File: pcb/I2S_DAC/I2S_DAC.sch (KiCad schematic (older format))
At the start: 36 parts, among them J1 AudioPlug3, J2 Conn_01x06, J3 Conn_01x09, U1 MIC5225-3.3YM5, U2 UDA1334ATS

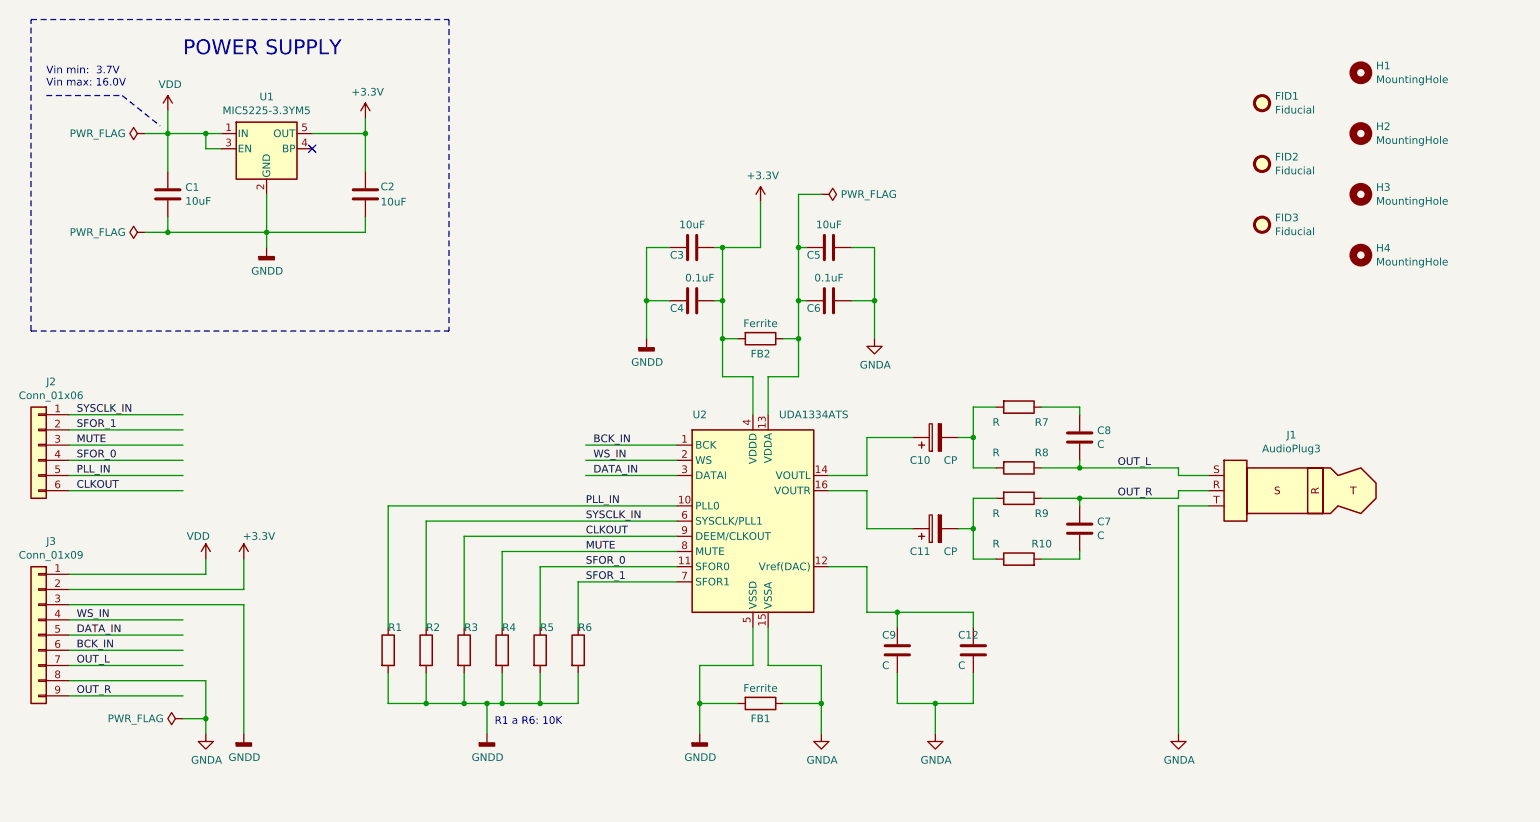
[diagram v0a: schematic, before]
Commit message: edicion de licencia en SCH
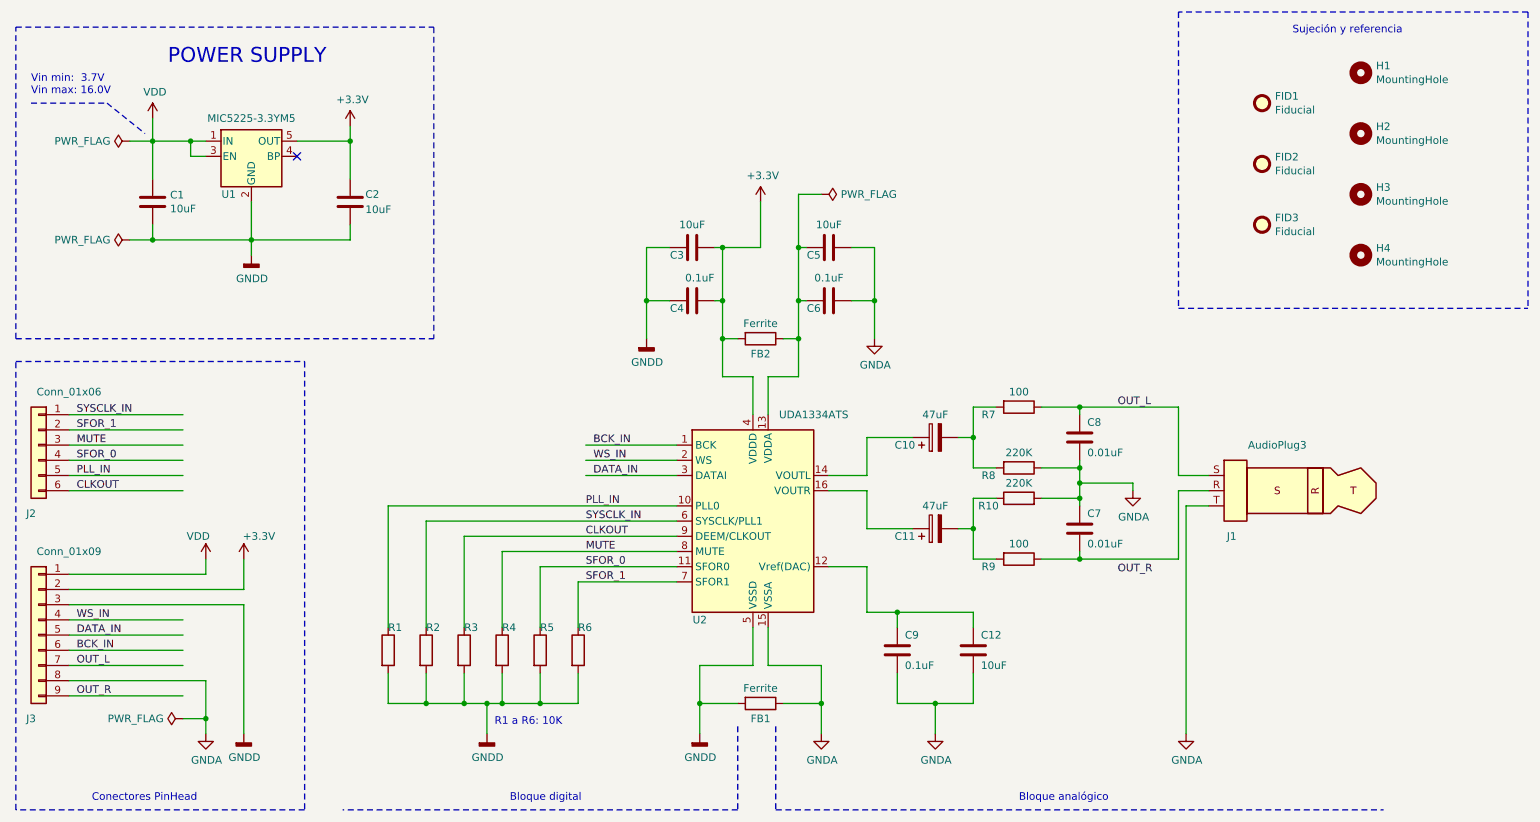
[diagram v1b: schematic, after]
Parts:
- C1, C2, C3, C4, C5, C6: footprint (none) -> Capacitor_SMD:C_0805_2012Metric
- C10, C11: value CP -> 47uF; footprint (none) -> Capacitor_SMD:C_Elec_4x5.4
- C12: value C -> 10uF; footprint (none) -> Capacitor_SMD:C_0805_2012Metric
- C7, C8: value C -> 0.01uF; footprint (none) -> Capacitor_SMD:C_0805_2012Metric
- C9: value C -> 0.1uF; footprint (none) -> Capacitor_SMD:C_0805_2012Metric
- FB1, FB2: footprint (none) -> Inductor_SMD:L_0805_2012Metric
- J2: footprint (none) -> Connector_PinHeader_2.54mm:PinHeader_1x06_P2.54mm_Vertical
- J3: footprint (none) -> Connector_PinHeader_2.54mm:PinHeader_1x09_P2.54mm_Vertical
- R1, R2, R3, R4, R5, R6: footprint (none) -> Resistor_SMD:R_0805_2012Metric
- R10, R8: value R -> 220K; footprint (none) -> Resistor_SMD:R_0805_2012Metric
- R7, R9: value R -> 100; footprint (none) -> Resistor_SMD:R_0805_2012Metric
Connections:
- wire segments 147 -> 151
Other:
- note added: "Bloque analógico"
- note added: "Bloque digital"
- note added: "Conectores PinHead"
- note added: "Sujeción y referencia"
- moved on the sheet: C1, C2, R10, R9, U1

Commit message: Archivos finales presentacion 14-10-2021
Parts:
- FB1, FB2: Codigo Mouser (none) -> 623-2508052217Y3
- J1: footprint Connector_Audio:Jack_3.5mm_CUI_SJ-3523-SMT_Horizontal -> Connector_Audio:Jack_3.5mm_CUI_SJ-3524-SMT_Horizontal; Codigo fabricante (none) -> SJ-3524-SMT-TR
- U1: Codigo fabricante (none) -> MIC5225-3.3YM5-TR
- U2: Codigo fabricante (none) -> UDA1334BTSN2112
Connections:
- wire segments 151 -> 153
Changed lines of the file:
@@
 F 1 "MIC5225-3.3YM5" H 2650 1850 50  0000 C CNN
 F 2 "Package_TO_SOT_SMD:SOT-23-5" H 2650 1925 50  0001 C CNN
-F 3 "http://ww1.microchip.com/downloads/en/DeviceDoc/20005785A.pdf" H 2650 1600 50  0001 C CNN
+F 3 "https://www.mouser.cl/datasheet/2/268/mic5225-1082288.pdf" H 2650 1600 50  0001 C CNN
+F 4 "MIC5225-3.3YM5-TR" H 2650 1600 50  0001 C CNN "Codigo fabricante"
 	1    2650 1600
 	1    0    0    -1
@@
 F 0 "J1" H 10000 3500 50  0000 C CNN
 F 1 "AudioPlug3" H 9700 4100 50  0000 C CNN
-F 2 "Connector_Audio:Jack_3.5mm_CUI_SJ-3523-SMT_Horizontal" H 9650 3750 50  0001 C CNN
-F 3 "~" H 9650 3750 50  0001 C CNN
+F 2 "Connector_Audio:Jack_3.5mm_CUI_SJ-3524-SMT_Horizontal" H 9650 3750 50  0001 C CNN
+F 3 "https://www.mouser.cl/datasheet/2/670/sj_352x_smt-1779397.pdf" H 9650 3750 50  0001 C CNN
+F 4 "SJ-3524-SMT-TR" H 9550 3800 50  0001 C CNN "Codigo fabricante"
 	1    9550 3800
 	-1   0    0    -1
@@
 F 2 "Package_SO:SSOP-16_4.4x5.2mm_P0.65mm" H 5950 4000 50  0001 C CNN
 F 3 "http://www.nxp.com/docs/en/data-sheet/UDA1334ATS.pdf" H 5950 4000 50  0001 C CNN
+F 4 "UDA1334BTSN2112" H 5950 4000 50  0001 C CNN "Codigo fabricante"
 	1    5950 4000
 	1    0    0    -1
@@
 P 1250 3500
 F 0 "J2" H 1300 3050 50  0000 C CNN
-F 1 "Conn_01x06" H 1050 3850 50  0000 C CNN
+F 1 "Conn_01x06" H 1050 3850 50  0001 C CNN
 F 2 "Connector_PinHeader_2.54mm:PinHeader_1x06_P2.54mm_Vertical" H 1250 3500 50  0001 C CNN
 F 3 "~" H 1250 3500 50  0001 C CNN
@@
 P 1250 4750
 F 0 "J3" H 1300 4200 50  0000 C CNN
-F 1 "Conn_01x09" H 1050 5300 50  0000 C CNN
+F 1 "Conn_01x09" H 1100 4250 50  0001 C CNN
 F 2 "Connector_PinHeader_2.54mm:PinHeader_1x09_P2.54mm_Vertical" H 1250 4750 50  0001 C CNN
 F 3 "~" H 1250 4750 50  0001 C CNN
@@
 F 1 "Ferrite" V 5900 2800 50  0000 C CNN
 F 2 "Inductor_SMD:L_0805_2012Metric" V 5930 2800 50  0001 C CNN
-F 3 "~" H 6000 2800 50  0001 C CNN
+F 3 "https://www.fair-rite.com/product/chip-beads-2508052217y3/?__cf_chl_managed_tk__=pmd_YvkcKczz8bbWuLTnNtKHP.MW17EIK.3JxHDwzraksHs-1632435725-0-gqNtZGzNAtCjcnBszRD9" H 6000 2800 50  0001 C CNN
+F 4 "623-2508052217Y3" V 6000 2800 50  0001 C CNN "Codigo Mouser"
 	1    6000 2800
 	0    1    1    0
@@
 F 1 "Ferrite" V 5900 5200 50  0000 C CNN
 F 2 "Inductor_SMD:L_0805_2012Metric" V 5930 5200 50  0001 C CNN
-F 3 "~" H 6000 5200 50  0001 C CNN
+F 3 "https://www.fair-rite.com/product/chip-beads-2508052217y3/?__cf_chl_managed_tk__=pmd_YvkcKczz8bbWuLTnNtKHP.MW17EIK.3JxHDwzraksHs-1632435725-0-gqNtZGzNAtCjcnBszRD9" H 6000 5200 50  0001 C CNN
+F 4 "623-2508052217Y3" V 6000 5200 50  0001 C CNN "Codigo Mouser"
 	1    6000 5200
 	0    1    1    0
@@
 	0    1    1    0
 $EndComp
-Text Label 8350 3250 0    50   ~ 0
+Text Label 8500 3250 0    50   ~ 0
 OUT_L
 Wire Wire Line
@@
 SFOR_1
 Wire Wire Line
-	2200 3300 1450 3300
-Wire Wire Line
-	2200 3400 1450 3400
-Wire Wire Line
-	2200 3500 1450 3500
-Wire Wire Line
-	2200 3600 1450 3600
-Wire Wire Line
-	2200 3700 1450 3700
-Wire Wire Line
-	2200 3800 1450 3800
+	1550 3300 1450 3300
+Wire Wire Line
+	1550 3400 1450 3400
+Wire Wire Line
+	1550 3500 1450 3500
+Wire Wire Line
+	1550 3600 1450 3600
+Wire Wire Line
+	1550 3700 1450 3700
+Wire Wire Line
+	1550 3800 1450 3800
 Wire Notes Line
 	3850 750  3850 2800
@@
 Wire Wire Line
 	4850 3700 5450 3700
-Text Label 4900 3500 0    50   ~ 0
+Text Label 4850 3500 0    50   ~ 0
 BCK_IN
-Text Label 4900 3600 0    50   ~ 0
+Text Label 4850 3600 0    50   ~ 0
 WS_IN
-Text Label 4900 3700 0    50   ~ 0
+Text Label 4850 3700 0    50   ~ 0
 DATA_IN
 Wire Wire Line
-	2200 4650 1450 4650
-Wire Wire Line
-	2200 4750 1450 4750
-Wire Wire Line
-	2200 4850 1450 4850
-Wire Wire Line
-	2200 4950 1450 4950
+	1550 4650 1450 4650
+Wire Wire Line
+	1550 4750 1450 4750
+Wire Wire Line
+	1550 4850 1450 4850
+Wire Wire Line
+	1550 4950 1450 4950
 $Comp
 L power:VDD #PWR0106
 U 1 1 61617A44
-P 2350 4250
-F 0 "#PWR0106" H 2350 4100 50  0001 C CNN
-F 1 "VDD" H 2300 4400 50  0000 C CNN
-F 2 "" H 2350 4250 50  0001 C CNN
-F 3 "" H 2350 4250 50  0001 C CNN
-	1    2350 4250
+P 1950 4150
+F 0 "#PWR0106" H 1950 4000 50  0001 C CNN
+F 1 "VDD" H 1900 4300 50  0000 C CNN
+F 2 "" H 1950 4150 50  0001 C CNN
+F 3 "" H 1950 4150 50  0001 C CNN
+	1    1950 4150
 	1    0    0    -1
 $EndComp
@@
 L power:+3.3V #PWR0107
 U 1 1 6161807E
-P 2600 4250
-F 0 "#PWR0107" H 2600 4100 50  0001 C CNN
-F 1 "+3.3V" H 2700 4400 50  0000 C CNN
-F 2 "" H 2600 4250 50  0001 C CNN
-F 3 "" H 2600 4250 50  0001 C CNN
-	1    2600 4250
+P 2200 4150
+F 0 "#PWR0107" H 2200 4000 50  0001 C CNN
+F 1 "+3.3V" H 2300 4300 50  0000 C CNN
+F 2 "" H 2200 4150 50  0001 C CNN
+F 3 "" H 2200 4150 50  0001 C CNN
+	1    2200 4150
 	1    0    0    -1
 $EndComp
@@
 L power:GNDD #PWR0108
 U 1 1 6163CFE5
-P 2600 5400
-F 0 "#PWR0108" H 2600 5150 50  0001 C CNN
-F 1 "GNDD" H 2604 5245 50  0000 C CNN
-F 2 "" H 2600 5400 50  0001 C CNN
-F 3 "" H 2600 5400 50  0001 C CNN
-	1    2600 5400
-	1    0    0    -1
-$EndComp
-Wire Wire Line
-	1450 4550 2600 4550
+P 2200 5400
+F 0 "#PWR0108" H 2200 5150 50  0001 C CNN
+F 1 "GNDD" H 2204 5245 50  0000 C CNN
+F 2 "" H 2200 5400 50  0001 C CNN
+F 3 "" H 2200 5400 50  0001 C CNN
+	1    2200 5400
+	1    0    0    -1
+$EndComp
+Wire Wire Line
+	1450 4550 2200 4550
 $Comp
 L power:GNDA #PWR0109
 U 1 1 61643A0A
-P 2350 5400
-F 0 "#PWR0109" H 2350 5150 50  0001 C CNN
-F 1 "GNDA" H 2355 5227 50  0000 C CNN
-F 2 "" H 2350 5400 50  0001 C CNN
-F 3 "" H 2350 5400 50  0001 C CNN
-	1    2350 5400
-	1    0    0    -1
-$EndComp
-Wire Wire Line
-	1450 5050 2350 5050
-Text Label 1500 4950 0    50   ~ 0
+P 1950 5400
+F 0 "#PWR0109" H 1950 5150 50  0001 C CNN
+F 1 "GNDA" H 1955 5227 50  0000 C CNN
+F 2 "" H 1950 5400 50  0001 C CNN
+F 3 "" H 1950 5400 50  0001 C CNN
+	1    1950 5400
+	1    0    0    -1
+$EndComp
+Wire Wire Line
+	1450 5050 1950 5050
+Text Label 1550 4950 0    50   ~ 0
 OUT_L
-Text Label 1500 4850 0    50   ~ 0
+Text Label 1550 4850 0    50   ~ 0
 BCK_IN
-Text Label 1500 4750 0    50   ~ 0
+Text Label 1550 4650 0    50   ~ 0
 DATA_IN
-Text Label 1500 4650 0    50   ~ 0
+Text Label 1550 4750 0    50   ~ 0
 WS_IN
-Text Label 1500 3300 0    50   ~ 0
+Text Label 1550 3300 0    50   ~ 0
 SYSCLK_IN
-Text Label 1500 3400 0    50   ~ 0
+Text Label 1550 3400 0    50   ~ 0
 SFOR_1
-Text Label 1500 3500 0    50   ~ 0
+Text Label 1550 3500 0    50   ~ 0
 MUTE
-Text Label 1500 3600 0    50   ~ 0
+Text Label 1550 3600 0    50   ~ 0
 SFOR_0
-Text Label 1500 3700 0    50   ~ 0
+Text Label 1550 3700 0    50   ~ 0
 PLL_IN
-Text Label 1500 3800 0    50   ~ 0
+Text Label 1550 3800 0    50   ~ 0
 CLKOUT
 Wire Wire Line
@@
 Connection ~ 5600 5200
 Wire Wire Line
-	2350 5400 2350 5300
-Wire Wire Line
-	2600 5400 2600 4550
-Wire Wire Line
-	2600 4450 2600 4250
-Wire Wire Line
-	1450 4450 2600 4450
-Wire Wire Line
-	2350 4350 2350 4250
-Wire Wire Line
-	1450 4350 2350 4350
+	1950 5400 1950 5300
+Wire Wire Line
+	2200 5400 2200 5300
+Wire Wire Line
+	1450 4450 2200 4450
+Wire Wire Line
+	1450 4350 1950 4350
 $Comp
 L power:+3.3V #PWR0110
@@
 L power:PWR_FLAG #FLG0101
 U 1 1 616812B1
-P 1850 1500
-F 0 "#FLG0101" H 1850 1575 50  0001 C CNN
-F 1 "PWR_FLAG" V 1850 1627 50  0000 L CNN
-F 2 "" H 1850 1500 50  0001 C CNN
-F 3 "~" H 1850 1500 50  0001 C CNN
-	1    1850 1500
+P 1900 4250
+F 0 "#FLG0101" H 1900 4325 50  0001 C CNN
+F 1 "PWR_FLAG" V 1900 4377 50  0000 L CNN
+F 2 "" H 1900 4250 50  0001 C CNN
+F 3 "~" H 1900 4250 50  0001 C CNN
+	1    1900 4250
 	0    -1   -1   0
 $EndComp
@@
 L power:PWR_FLAG #FLG0102
 U 1 1 61681F39
-P 1850 2150
-F 0 "#FLG0102" H 1850 2225 50  0001 C CNN
-F 1 "PWR_FLAG" V 1850 2277 50  0000 L CNN
-F 2 "" H 1850 2150 50  0001 C CNN
-F 3 "~" H 1850 2150 50  0001 C CNN
-	1    1850 2150
-	0    -1   -1   0
-$EndComp
-Wire Wire Line
-	1850 2150 2000 2150
-Connection ~ 2000 2150
-Wire Wire Line
-	1850 1500 2000 1500
+P 2250 5300
+F 0 "#FLG0102" H 2250 5375 50  0001 C CNN
+F 1 "PWR_FLAG" V 2350 5350 50  0000 L CNN
+F 2 "" H 2250 5300 50  0001 C CNN
+F 3 "~" H 2250 5300 50  0001 C CNN
+	1    2250 5300
+	0    1    1    0
+$EndComp
 $Comp
 L power:PWR_FLAG #FLG0103
 U 1 1 6168E4B2
-P 2200 5300
-F 0 "#FLG0103" H 2200 5375 50  0001 C CNN
-F 1 "PWR_FLAG" V 2200 5427 50  0000 L CNN
-F 2 "" H 2200 5300 50  0001 C CNN
-F 3 "~" H 2200 5300 50  0001 C CNN
-	1    2200 5300
+P 1800 5300
+F 0 "#FLG0103" H 1800 5375 50  0001 C CNN
+F 1 "PWR_FLAG" V 1700 5250 50  0000 L CNN
+F 2 "" H 1800 5300 50  0001 C CNN
+F 3 "~" H 1800 5300 50  0001 C CNN
+	1    1800 5300
 	0    -1   -1   0
 $EndComp
 Wire Wire Line
-	2200 5300 2350 5300
-Connection ~ 2350 5300
-Wire Wire Line
-	2350 5300 2350 5050
+	1800 5300 1950 5300
 $Comp
 L power:PWR_FLAG #FLG0104
@@
 Wire Wire Line
 	8800 3900 8950 3900
-Text Label 8350 4350 0    50   ~ 0
+Text Label 8500 4250 0    50   ~ 0
 OUT_R
 Wire Wire Line
-	2200 5150 1450 5150
-Text Label 1500 5150 0    50   ~ 0
+	1550 5150 1450 5150
+Text Label 1550 5150 0    50   ~ 0
 OUT_R
 Wire Notes Line
@@
 Bloque digital
 Wire Notes Line
-	3000 2950 3000 5900
-Wire Notes Line
-	3000 5900 1100 5900
+	2900 2950 2900 5900
 Wire Notes Line
 	1100 5900 1100 2950
-Wire Notes Line
-	1100 2950 3000 2950
 Text Notes 1600 5850 0    50   ~ 0
 Conectores PinHead
@@
 Text Notes 9500 800  0    50   ~ 0
 Sujeción y referencia
+Wire Wire Line
+	1950 4150 1950 4250
+Wire Wire Line
+	2200 4150 2200 4450
+Wire Wire Line
+	1950 5300 1950 5050
+Connection ~ 1950 5300
+Wire Wire Line
+	1900 4250 1950 4250
+Connection ~ 1950 4250
+Wire Wire Line
+	1950 4250 1950 4350
+Wire Wire Line
+	2250 5300 2200 5300
+Connection ~ 2200 5300
+Wire Wire Line
+	2200 5300 2200 4550
+Wire Notes Line
+	2900 2950 1100 2950
+Wire Notes Line
+	2900 5900 1100 5900
 $EndSCHEMATC
